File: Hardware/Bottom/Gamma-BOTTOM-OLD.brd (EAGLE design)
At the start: 33 x 33 mm, 36 parts, among them U4 PCF8523

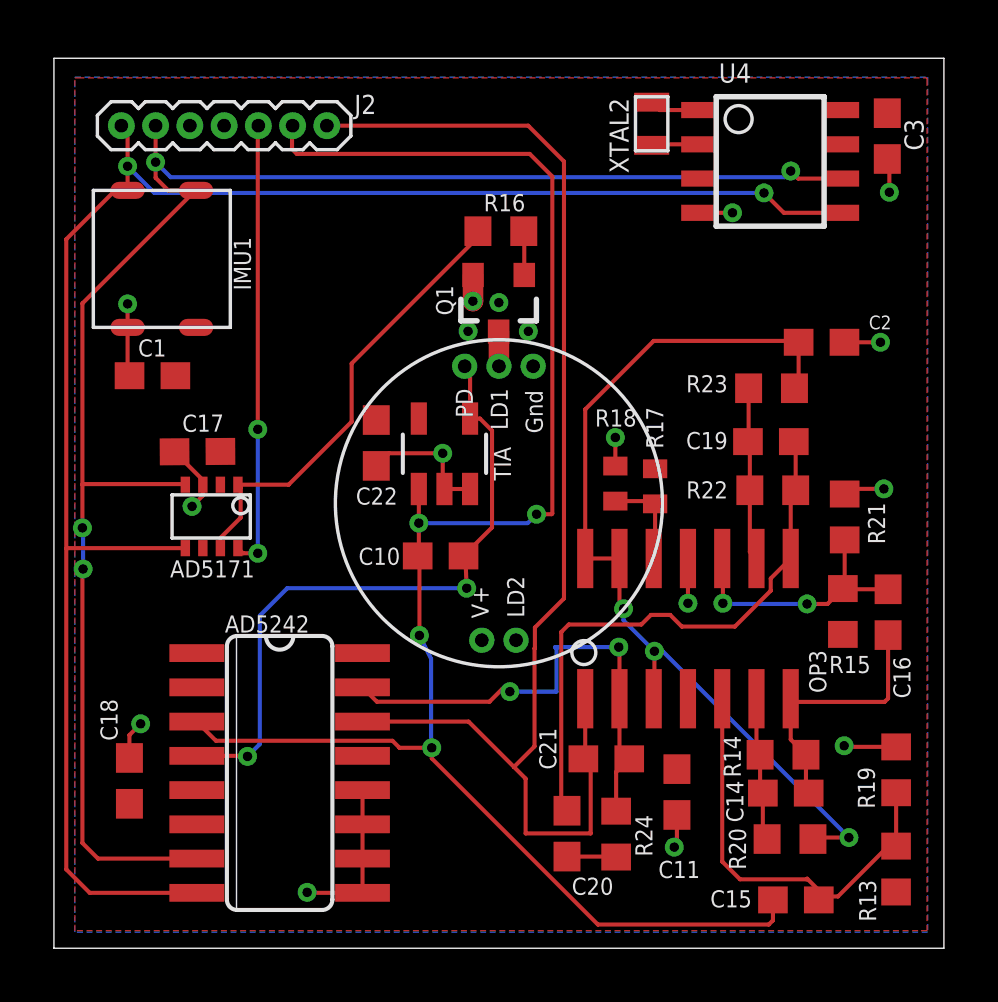
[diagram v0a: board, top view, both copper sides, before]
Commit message: Updated file names and completed preliminary BOM for each board
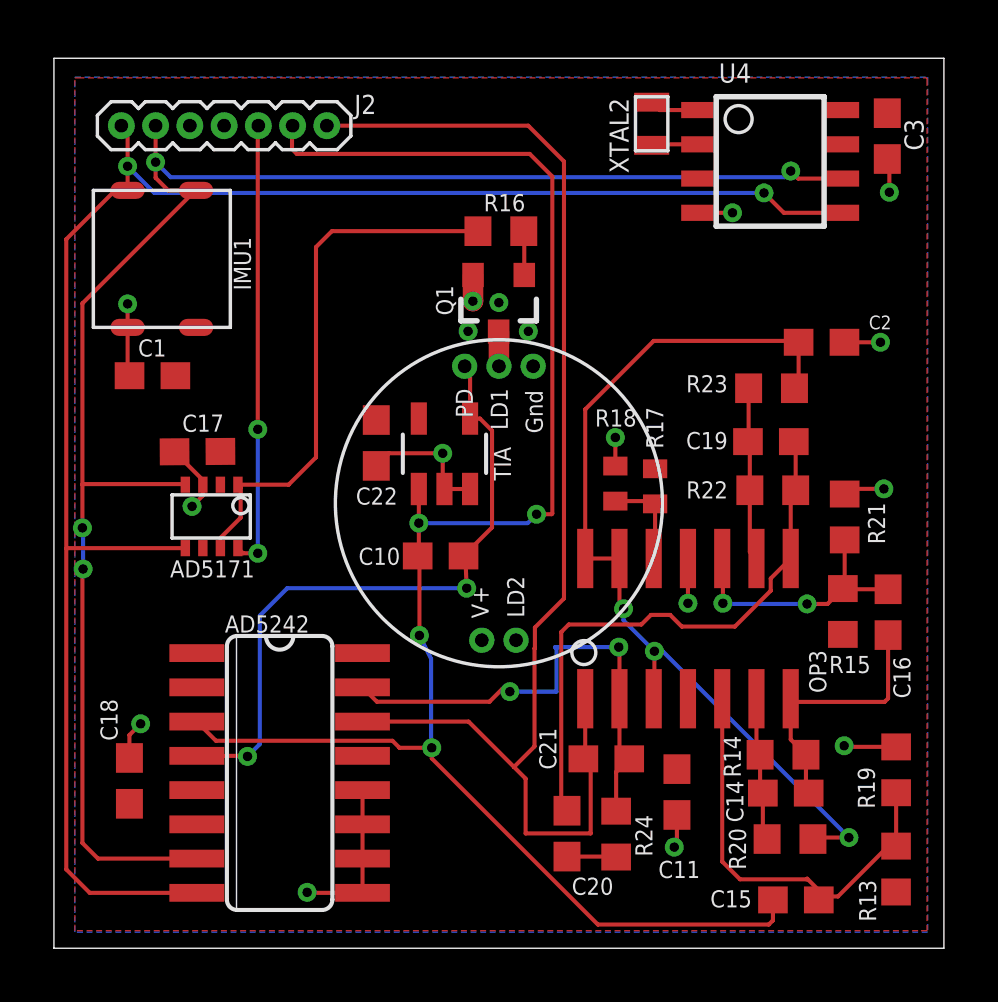
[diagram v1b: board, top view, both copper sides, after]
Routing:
- net N$9: track 16.9 -> 20.1 mm
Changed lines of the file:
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@@
 <contactref element="AD5171" pad="1"/>
 <contactref element="R16" pad="1"/>
-<wire x1="13.5382" y1="22.023115625" x2="11.202484375" y2="19.6874" width="0.1524" layer="1"/>
+<wire x1="12.2174" y1="20.702315625" x2="11.202484375" y2="19.6874" width="0.1524" layer="1"/>
 <wire x1="9.3218" y1="19.6874" x2="11.202484375" y2="19.6874" width="0.1524" layer="1"/>
-<wire x1="13.5382" y1="24.1808" x2="13.5382" y2="22.023115625" width="0.1524" layer="1"/>
-<wire x1="18.2216" y1="29.0886" x2="18.2216" y2="28.8642" width="0.1524" layer="1"/>
-<wire x1="18.2216" y1="28.8642" x2="13.5382" y2="24.1808" width="0.1524" layer="1"/>
+<wire x1="12.2174" y1="20.702315625" x2="12.2174" y2="28.4988" width="0.1524" layer="1"/>
+<wire x1="12.2174" y1="28.4988" x2="12.8072" y2="29.0886" width="0.1524" layer="1"/>
+<wire x1="12.8072" y1="29.0886" x2="18.2216" y2="29.0886" width="0.1524" layer="1"/>
 <wire x1="8.6718" y1="17.3346" x2="8.6718" y2="17.7142" width="0.1524" layer="1"/>
 <wire x1="8.6718" y1="17.7142" x2="9.4234" y2="18.4658" width="0.1524" layer="1"/>

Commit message: small fixes
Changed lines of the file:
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@@
 <?xml version="1.0" encoding="utf-8"?>
 <!DOCTYPE eagle SYSTEM "eagle.dtd">
-<eagle version="9.5.2">
+<eagle version="9.6.2">
 <drawing>
 <settings>
@@
 <wire x1="10.0584" y1="17.145" x2="9.5114" y2="17.145" width="0.1524" layer="1"/>
 <wire x1="9.5114" y1="17.145" x2="9.3218" y2="17.3346" width="0.1524" layer="1"/>
-<wire x1="10.0584" y1="17.145" x2="10.0584" y2="21.7424" width="0.1524" layer="16"/>
-<via x="10.0584" y="21.7424" extent="1-16" drill="0.35"/>
-<wire x1="10.0584" y1="21.7424" x2="10.0584" y2="32.9784" width="0.1524" layer="1"/>
-<wire x1="10.0584" y1="32.9784" x2="10.08" y2="33" width="0.1524" layer="1"/>
+<wire x1="10.0076" y1="23.4188" x2="10.0076" y2="17.1958" width="0.1524" layer="16"/>
+<wire x1="10.0584" y1="17.145" x2="10.0076" y2="17.1958" width="0.1524" layer="16"/>
+<via x="10.0076" y="23.4188" extent="1-16" drill="0.35"/>
+<wire x1="10.0076" y1="23.4188" x2="10.0076" y2="32.9276" width="0.1524" layer="1"/>
+<wire x1="10.0076" y1="32.9276" x2="10.08" y2="33" width="0.1524" layer="1"/>
 </signal>
 </signals>
